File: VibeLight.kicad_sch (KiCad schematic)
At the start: 0 parts

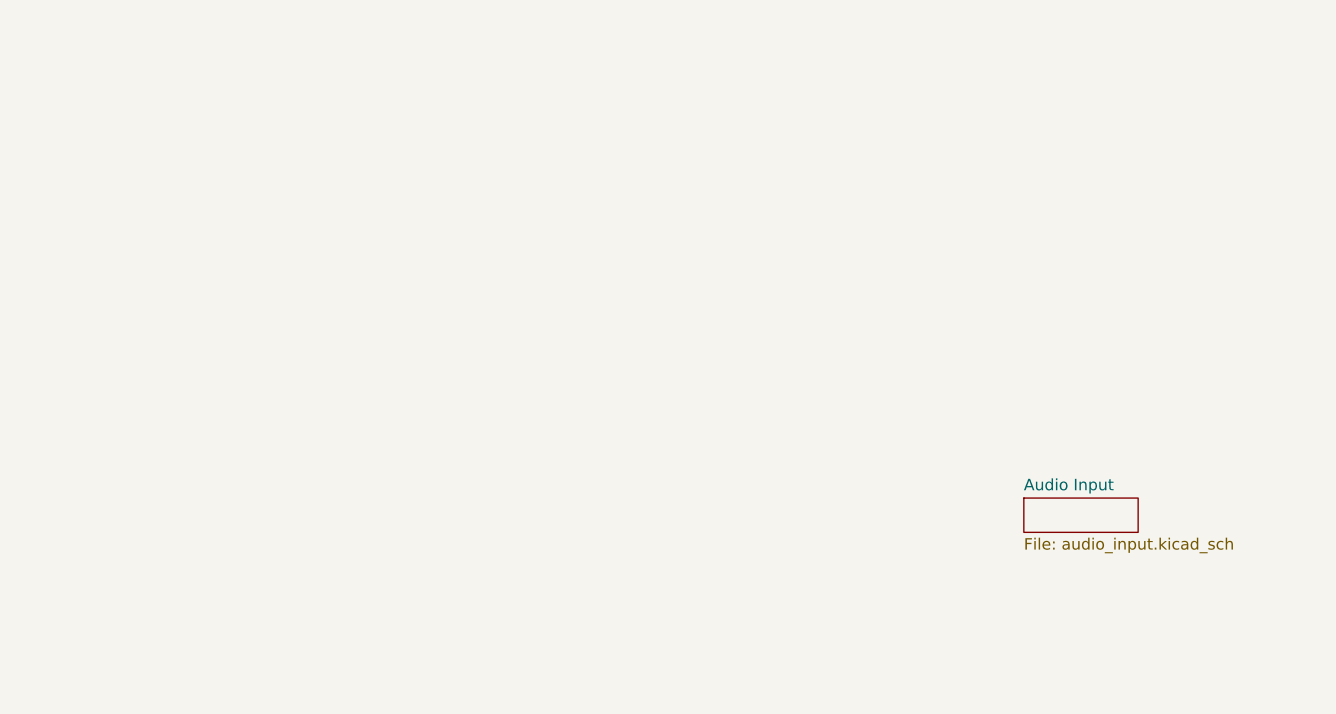
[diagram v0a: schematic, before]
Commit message: Rev 1
needs sensors, things like pull-up resistors and protection diodes, electrical rules check. also check SCL and SDA busses, variable resistors
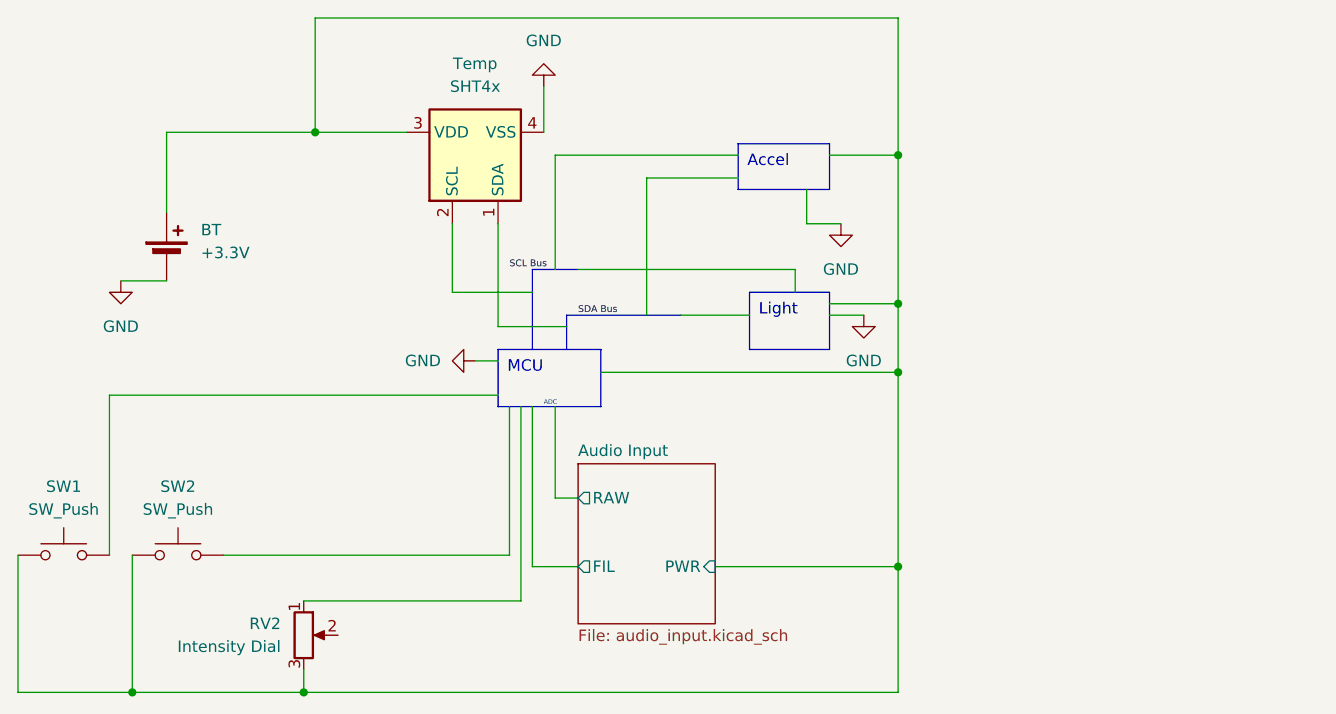
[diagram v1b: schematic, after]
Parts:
- added BT: +3.3V, symbol Device:Battery_Cell
- added RV2: Intensity Dial, Potentiometer_SMD:Potentiometer_ACP_CA6-VSMD_Vertical, symbol Device:R_Potentiometer
- added SW1, SW2: SW_Push, symbol Switch:SW_Push
- added Temp: SHT4x, Sensor_Humidity:Sensirion_DFN-4_1.5x1.5mm_P0.8mm_SHT4x_NoCentralPad, symbol Sensor_Humidity:SHT4x
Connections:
- new net Audio Input/PWR: BT.1 (+), RV2.3, SW1.1, SW2.1, Temp.3 (VDD)
- new net GND: BT.2 (-), Temp.4 (VSS)
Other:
- sheet Audio Input ports: added FIL, PWR, RAW; removed none
- note added: "ADC"

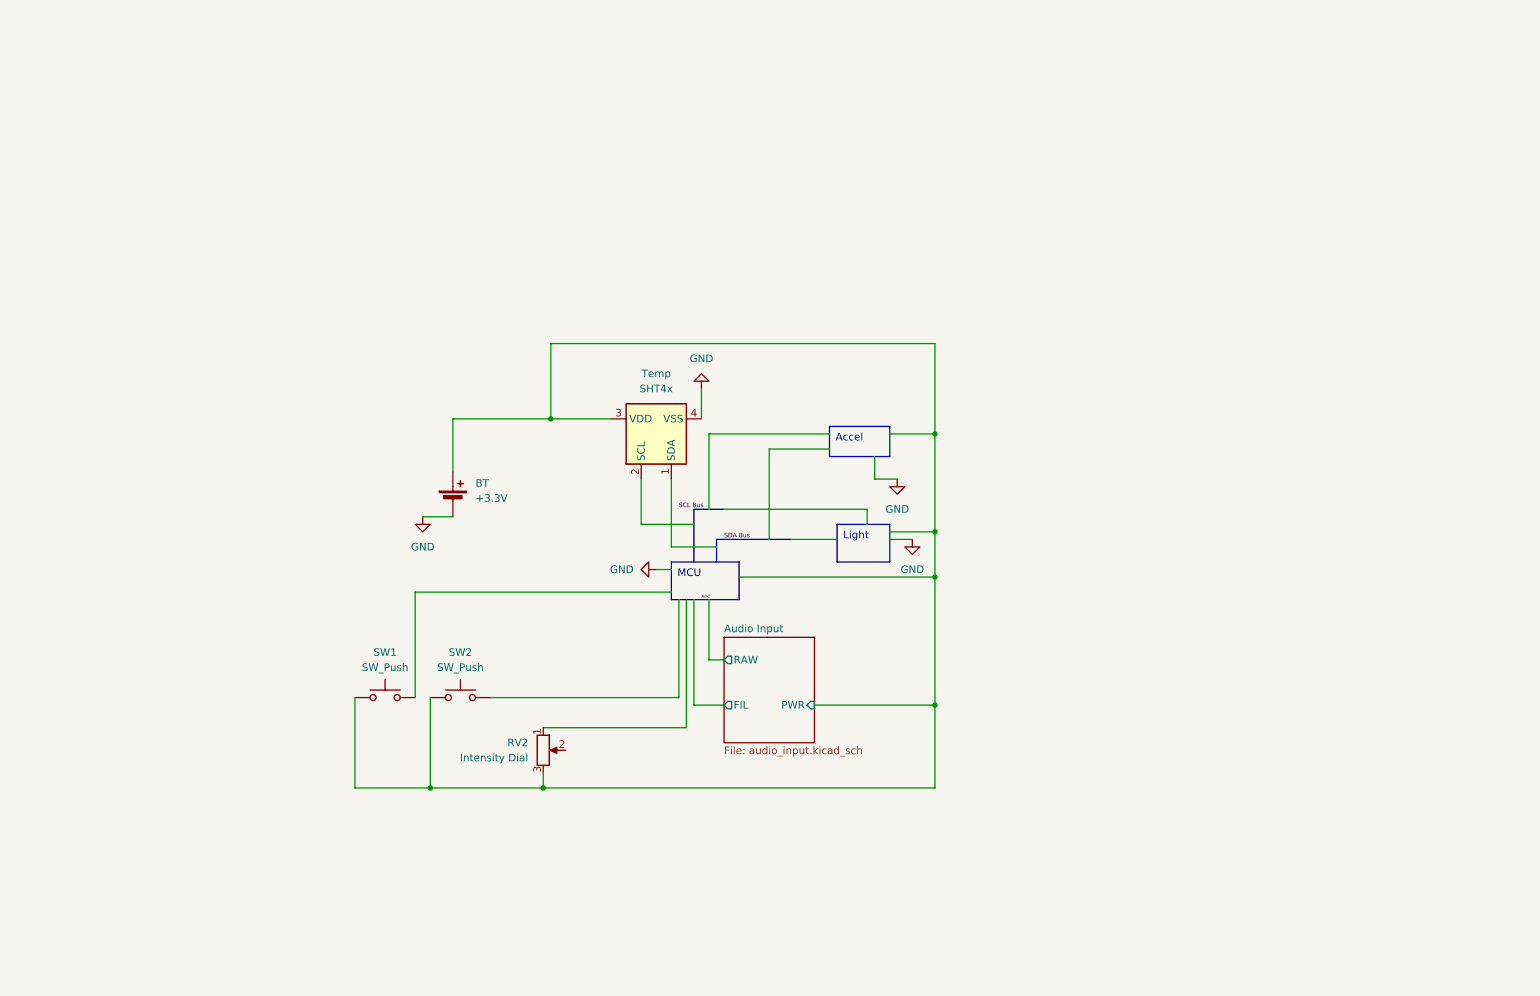
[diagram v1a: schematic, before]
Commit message: added some components
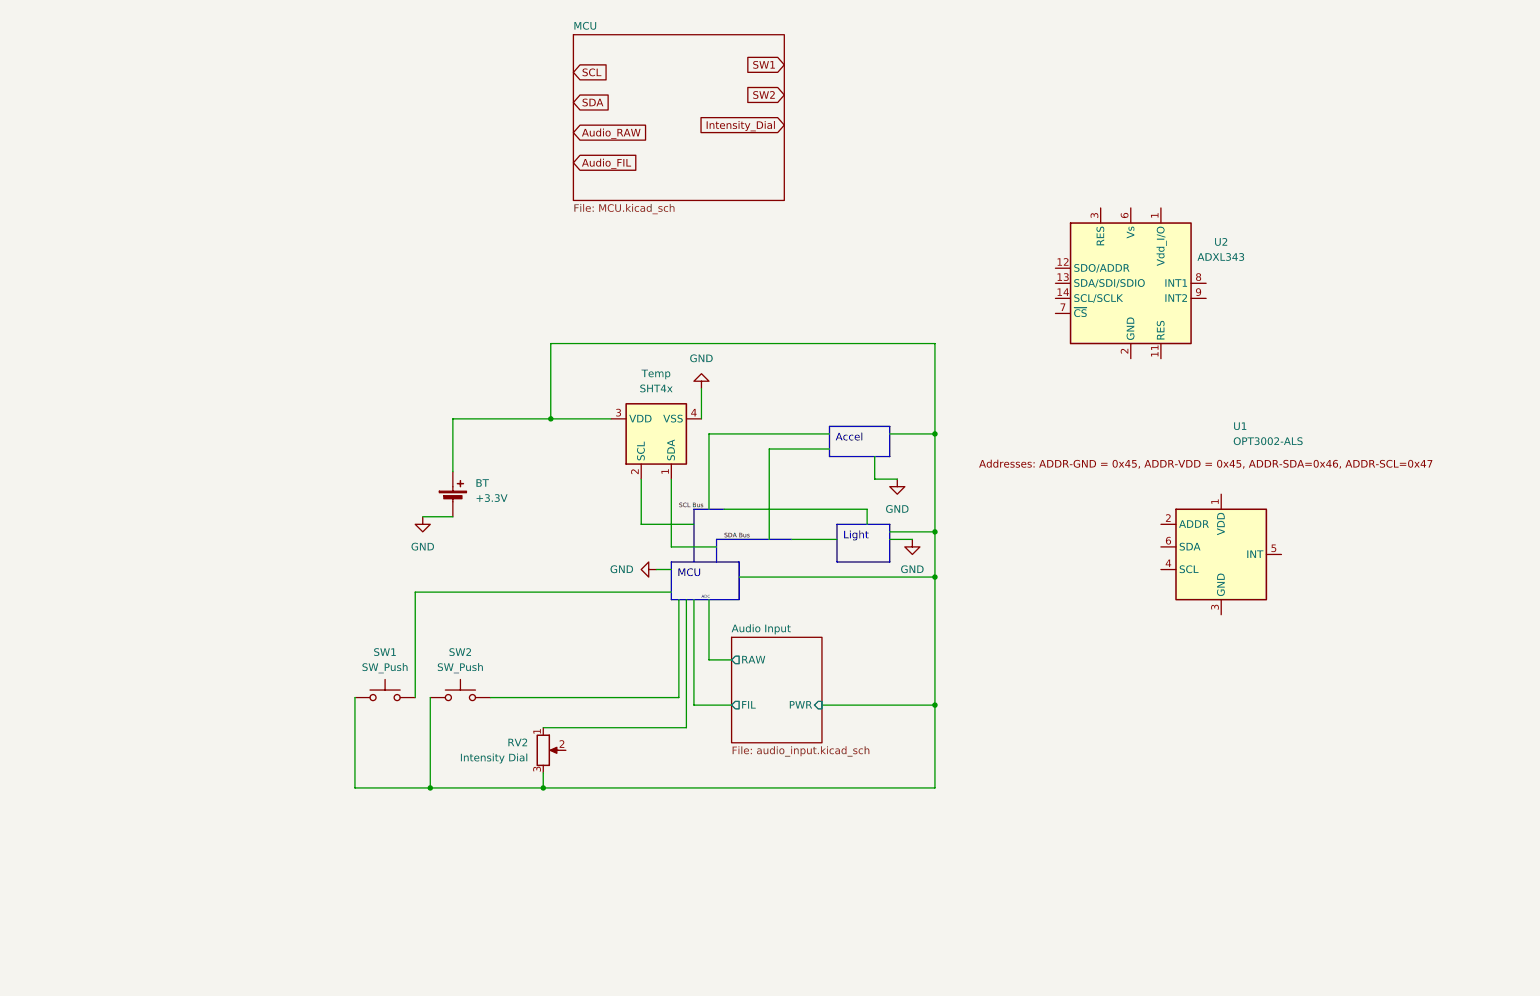
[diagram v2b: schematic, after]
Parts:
- added U1: OPT3002-ALS, OptoDevice:SON65P200X200X65-7N, symbol Sensor_Optical:OPT3002-ALS
- added U2: ADXL343, Package_LGA:LGA-14_3x5mm_P0.8mm_LayoutBorder1x6y, symbol Sensor_Motion:ADXL343
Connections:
- new net: U2.2 (GND), U2.4 (GND), U2.5 (GND)
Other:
- added sheet MCU (MCU.kicad_sch)
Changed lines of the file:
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@@
   (junction (at 90.17 154.94) (diameter 0) (color 0 0 0 0)
   )
-  (wire (pts (xy 139.7 133.35) (xy 137.16 133.35))
+  (wire (pts (xy 140.97 133.35) (xy 137.16 133.35))
     (stroke (width 0) (type default))
   )
@@
     (stroke (width 0) (type default))
   )
-  (wire (pts (xy 154.94 140.97) (xy 175.26 140.97))
+  (wire (pts (xy 156.21 140.97) (xy 175.26 140.97))
     (stroke (width 0) (type default))
   )
@@
     (stroke (width 0) (type default))
   )
-  (wire (pts (xy 139.7 140.97) (xy 134.62 140.97))
+  (wire (pts (xy 140.97 140.97) (xy 134.62 140.97))
     (stroke (width 0) (type default))
   )
@@
     (effects (font (size 0.75 0.75)) (justify left bottom))
   )
+  (global_label "SCL" (shape input) (at 114.3 34.29 0) (fields_autoplaced)
+    (effects (font (size 1.27 1.27)) (justify left))
+    (property "Intersheetrefs" "${INTERSHEET_REFS}" (at 120.7928 34.29 0)
+      (effects (font (size 1.27 1.27)) (justify left) hide)
+    )
+  )
+  (global_label "SDA" (shape input) (at 114.3 39.37 0) (fields_autoplaced)
+    (effects (font (size 1.27 1.27)) (justify left))
+    (property "Intersheetrefs" "${INTERSHEET_REFS}" (at 120.8533 39.37 0)
+      (effects (font (size 1.27 1.27)) (justify left) hide)
+    )
+  )
+  (global_label "Audio_RAW" (shape input) (at 114.3 44.45 0) (fields_autoplaced)
+    (effects (font (size 1.27 1.27)) (justify left))
+    (property "Intersheetrefs" "${INTERSHEET_REFS}" (at 127.2032 44.45 0)
+      (effects (font (size 1.27 1.27)) (justify left) hide)
+    )
+  )
+  (global_label "Audio_FIL" (shape input) (at 114.3 49.53 0) (fields_autoplaced)
+    (effects (font (size 1.27 1.27)) (justify left))
+    (property "Intersheetrefs" "${INTERSHEET_REFS}" (at 126.1147 49.53 0)
+      (effects (font (size 1.27 1.27)) (justify left) hide)
+    )
+  )
+  (global_label "SW2" (shape input) (at 149.86 38.1 180) (fields_autoplaced)
+    (effects (font (size 1.27 1.27)) (justify right))
+    (property "Intersheetrefs" "${INTERSHEET_REFS}" (at 143.0044 38.1 0)
+      (effects (font (size 1.27 1.27)) (justify right) hide)
+    )
+  )
+  (global_label "SW1" (shape input) (at 149.86 33.02 180) (fields_autoplaced)
+    (effects (font (size 1.27 1.27)) (justify right))
+    (property "Intersheetrefs" "${INTERSHEET_REFS}" (at 143.0044 33.02 0)
+      (effects (font (size 1.27 1.27)) (justify right) hide)
+    )
+  )
+  (global_label "Intensity_Dial" (shape input) (at 149.86 43.18 180) (fields_autoplaced)
+    (effects (font (size 1.27 1.27)) (justify right))
+    (property "Intersheetrefs" "${INTERSHEET_REFS}" (at 134.1749 43.18 0)
+      (effects (font (size 1.27 1.27)) (justify right) hide)
+    )
+  )
   (symbol (lib_id "Switch:SW_Push") (at 95.25 139.7 0) (unit 1)
     (in_bom yes) (on_board yes) (dnp no) (fields_autoplaced)
@@
     )
   )
+  (symbol (lib_id "Sensor_Motion:ADXL343") (at 208.28 69.85 0) (unit 1)
+    (in_bom yes) (on_board yes) (dnp no) (fields_autoplaced)
+    (property "Reference" "U2" (at 223.52 62.9219 0)
+      (effects (font (size 1.27 1.27)))
+    )
+    (property "Value" "ADXL343" (at 223.52 65.4619 0)
+      (effects (font (size 1.27 1.27)))
+    )
+    (property "Footprint" "Package_LGA:LGA-14_3x5mm_P0.8mm_LayoutBorder1x6y" (at 208.28 69.85 0)
+      (effects (font (size 1.27 1.27)) hide)
+    )
+    (property "Datasheet" "https://www.analog.com/media/en/technical-documentation/data-sheets/ADXL343.pdf" (at 208.28 69.85 0)
+      (effects (font (size 1.27 1.27)) hide)
+    )
+    (pin "1")
+    (pin "10")
+    (pin "11")
+    (pin "12")
+    (pin "13")
+    (pin "14")
+    (pin "2")
+    (pin "3")
+    (pin "4")
+    (pin "5")
+    (pin "6")
+    (pin "7")
+    (pin "8")
+    (pin "9")
+    (instances
+      (project "VibeLight"
+        (path "/704dec10-a4c2-4298-be85-193d9407f59f"
+          (reference "U2") (unit 1)
+        )
+      )
+    )
+  )
   (symbol (lib_id "Switch:SW_Push") (at 82.55 139.7 0) (unit 1)
     (in_bom yes) (on_board yes) (dnp no) (fields_autoplaced)
@@
     )
   )
+  (symbol (lib_name "OPT3002-ALS_1") (lib_id "Sensor_Optical:OPT3002-ALS") (at 223.52 115.57 0) (unit 1)
+    (in_bom yes) (on_board yes) (dnp no) (fields_autoplaced)
+    (property "Reference" "U1" (at 225.5394 93.98 0)
+      (effects (font (size 1.27 1.27)) (justify left))
+    )
+    (property "Value" "OPT3002-ALS" (at 225.5394 96.52 0)
+      (effects (font (size 1.27 1.27)) (justify left))
+    )
+    (property "Footprint" "OptoDevice:SON65P200X200X65-7N" (at 223.52 102.87 0)
+      (effects (font (size 1.27 1.27)) hide)
+    )
+    (property "Datasheet" "https://www.ti.com/lit/ds/symlink/opt3002.pdf?ts=1686147829524&ref_url=https%253A%252F%252Fwww.ti.com%252Fproduct%252FOPT3002" (at 217.17 105.41 0)
+      (effects (font (size 1.27 1.27)) hide)
+    )
+    (pin "1")
+    (pin "2")
+    (pin "2")
+    (pin "3")
+    (pin "4")
+    (pin "5")
+    (pin "6")
+    (instances
+      (project "VibeLight"
+        (path "/704dec10-a4c2-4298-be85-193d9407f59f"
+          (reference "U1") (unit 1)
+        )
+      )
+      (project "Sensor-Board-Demo"
+        (path "/e63e39d7-6ac0-4ffd-8aa3-1841a4541b55"
+          (reference "U11") (unit 1)
+        )
+      )
+    )
+  )
   (symbol (lib_id "power:GND") (at 88.9 109.22 0) (unit 1)
     (in_bom yes) (on_board yes) (dnp no) (fields_autoplaced)
@@
     )
   )
-  (sheet (at 139.7 129.54) (size 15.24 17.78) (fields_autoplaced)
+  (sheet (at 140.97 129.54) (size 15.24 17.78) (fields_autoplaced)
     (stroke (width 0.1524) (type solid))
     (fill (color 0 0 0 0.0000))
-    (property "Sheetname" "Audio Input" (at 139.7 128.8284 0)
+    (property "Sheetname" "Audio Input" (at 140.97 128.8284 0)
       (effects (font (size 1.27 1.27)) (justify left bottom))
     )
-    (property "Sheetfile" "audio_input.kicad_sch" (at 139.7 147.9046 0)
+    (property "Sheetfile" "audio_input.kicad_sch" (at 140.97 147.9046 0)
       (effects (font (size 1.27 1.27)) (justify left top))
     )
-    (pin "RAW" output (at 139.7 133.35 180)
+    (pin "RAW" output (at 140.97 133.35 180)
       (effects (font (size 1.27 1.27)) (justify left))
     )
-    (pin "FIL" output (at 139.7 140.97 180)
+    (pin "FIL" output (at 140.97 140.97 180)
       (effects (font (size 1.27 1.27)) (justify left))
     )
-    (pin "PWR" input (at 154.94 140.97 0)
+    (pin "PWR" input (at 156.21 140.97 0)
       (effects (font (size 1.27 1.27)) (justify right))
     )
@@
       )
     )
+  )
+  (sheet (at 114.3 27.94) (size 35.56 27.94) (fields_autoplaced)
+    (stroke (width 0.1524) (type solid))
+    (fill (color 0 0 0 0.0000))
+    (property "Sheetname" "MCU" (at 114.3 27.2284 0)
+      (effects (font (size 1.27 1.27)) (justify left bottom))
+    )
+    (property "Sheetfile" "MCU.kicad_sch" (at 114.3 56.4646 0)
+      (effects (font (size 1.27 1.27)) (justify left top))
+    )
+    (instances
+      (project "VibeLight"
+        (path "/704dec10-a4c2-4298-be85-193d9407f59f" (page "3"))
+      )
+    )

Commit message: misc changes during call
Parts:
- removed BT: +3.3V, symbol Device:Battery_Cell
- added C3, C4: 100nF, Capacitor_SMD:C_0603_1608Metric_Pad1.08x0.95mm_HandSolder, symbol Device:C
- added J1: Conn_01x03_Pin, symbol Connector:Conn_01x03_Pin
- added J2: Conn_01x02, symbol Connector_Generic:Conn_01x02
- added R1, R2: xR, Resistor_SMD:R_0603_1608Metric_Pad0.98x0.95mm_HandSolder, symbol Device:R
- added U4: LK112M33TR, Package_TO_SOT_SMD:SOT-23-5, symbol Regulator_Linear:LK112M33TR
- RV2: footprint Potentiometer_SMD:Potentiometer_ACP_CA6-VSMD_Vertical -> Potentiometer_SMD:Potentiometer_Bourns_TC33X_Vertical; Source (none) -> https://www.digikey.com/en/products/detail/bourns-inc/TC33X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
- SW1, SW2: footprint (none) -> Button_Switch_SMD:SW_Push_1P1T_NO_CK_KMR2; Source (none) -> https://www.digikey.com/en/products/detail/c-k-va/KMR223GLF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
- renumbered Temp to Temp1
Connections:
- net GND: now also C3.2, C4.2, J1.3 (Pin_3), J2.1 (Pin_1), U4.2 (GND)
- net Intensity_Dial: now also RV2.2
- net +3V3: now reaches RV2.1
- net +3V3: now also Temp1.3 (VDD), U1.1 (VDD), U2.6 (Vs), C4.1, R1.1, R2.1, U4.4 (OUT)
- net ACCEL_INT1: now reaches U2.8 (INT1)
- net ACCEL_INT2: now reaches U2.9 (INT2)
- net OPT_INT: now reaches U1.5 (INT)
- net Audio Input/PWR renamed BATT+
- net BATT+: now also J2.2 (Pin_2), U4.1 (SHDN), U4.5 (IN); no longer Temp1.3 (VDD)
- new net: C3.1, U4.3 (Bypass)
- new net LED_CNTRL: J1.2 (Pin_2)
- new net LED_PWR: J1.1 (Pin_1)
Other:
- sheet MCU ports: added Audio_FIL, Intensity_Dial; removed none
- moved on the sheet: SW2, U1

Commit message: started work on pcb layout
started work on pcb layout
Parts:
- removed R1, R2: xR, Resistor_SMD:R_0603_1608Metric_Pad0.98x0.95mm_HandSolder, symbol Device:R
- added R3, R4, R5: R, Resistor_SMD:R_0603_1608Metric_Pad0.98x0.95mm_HandSolder, symbol Device:R
- renumbered U2 to Accel1, U1 to Light1, J1 to OUT_PINS1, J2 to PWR_IN1, U4 to PWR_REG1
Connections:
- net +3V3 is gone; now on net Audio Input/PWR: Accel1.6 (Vs), C4.1, Light1.1 (VDD), PWR_REG1.4 (OUT), RV2.1, Temp1.3 (VDD)
- net LED_PWR is gone; now on net Audio Input/PWR: OUT_PINS1.1 (Pin_1)
- net BATT+: no longer RV2.3, SW1.1, SW2.1
- net GND: now also Accel1.2 (GND), Accel1.4 (GND), Accel1.5 (GND), Light1.2 (NC), Light1.3 (GND), RV2.3
- net Audio Input/PWR: now reaches SW2.2
- net Audio Input/PWR: now also Accel1.7 (~{CS}), SW1.2, R3.1, R4.1, R5.1
- net ACCEL_INT1 renamed MCU/ACC_INT1
- net ACCEL_INT2 renamed MCU/ACC_INT2
- net Intensity_Dial renamed MCU/Intensity_Dial
- net LED_CNTRL renamed MCU/LED_CNTRL
- net OPT_INT renamed MCU/OPT_INT
- net MCU/OPT_INT: now also R5.2
- new net MCU/SW1: SW1.1
- new net MCU/SW2: SW2.1
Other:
- sheet MCU ports: added ACC_INT1, ACC_INT2, Audio_RAW, Battery, LED_CNTRL, OPT_INT, SCL, SDA, SW1, SW2; removed none
- note removed: "ADC"
- moved on the sheet: Accel1, C3, C4, Light1, OUT_PINS1, PWR_IN1, PWR_REG1, RV2, SW1, SW2, Temp1

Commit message: added OPT and JST footprints
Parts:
- Light1: footprint OptoDevice:SON65P200X200X65-7N -> OP3002:SON65P200X200X65-7N
- OUT_PINS1: footprint (none) -> Connector_JST:JST_GH_BM03B-GHS-TBT_1x03-1MP_P1.25mm_Vertical
- PWR_IN1: footprint (none) -> Connector_JST:JST_GH_BM02B-GHS-TBT_1x02-1MP_P1.25mm_Vertical
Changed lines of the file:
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@@
       (effects (font (size 1.27 1.27)))
     )
-    (property "Footprint" "" (at 233.68 63.5 0)
+    (property "Footprint" "Connector_JST:JST_GH_BM03B-GHS-TBT_1x03-1MP_P1.25mm_Vertical" (at 233.68 63.5 0)
       (effects (font (size 1.27 1.27)) hide)
     )
@@
       (effects (font (size 1.27 1.27)))
     )
-    (property "Footprint" "" (at 26.67 147.32 0)
+    (property "Footprint" "Connector_JST:JST_GH_BM02B-GHS-TBT_1x02-1MP_P1.25mm_Vertical" (at 26.67 147.32 0)
       (effects (font (size 1.27 1.27)) hide)
     )
@@
       (effects (font (size 1.27 1.27)) (justify left))
     )
-    (property "Footprint" "OptoDevice:SON65P200X200X65-7N" (at 212.09 100.33 0)
-      (effects (font (size 1.27 1.27)) hide)
-    )
+    (property "Footprint" "OP3002:SON65P200X200X65-7N" (at 212.09 100.33 0)
+      (effects (font (size 1.27 1.27)) hide)
+    )
